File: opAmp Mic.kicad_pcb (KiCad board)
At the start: 2 copper layers, 19 x 80.5 mm, 24 parts, among them J1 XLR3, U1 OPA1642

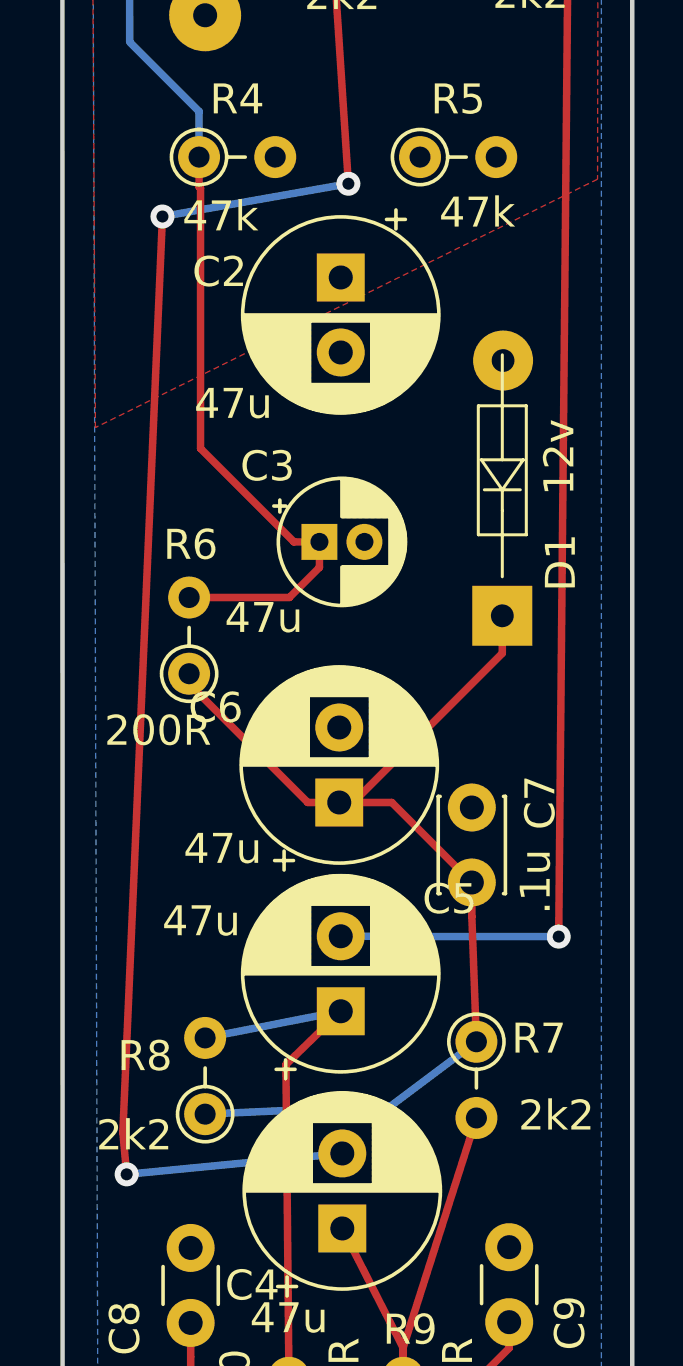
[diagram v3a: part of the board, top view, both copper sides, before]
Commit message: cleaned up 1 trace for only aesthetic reasons
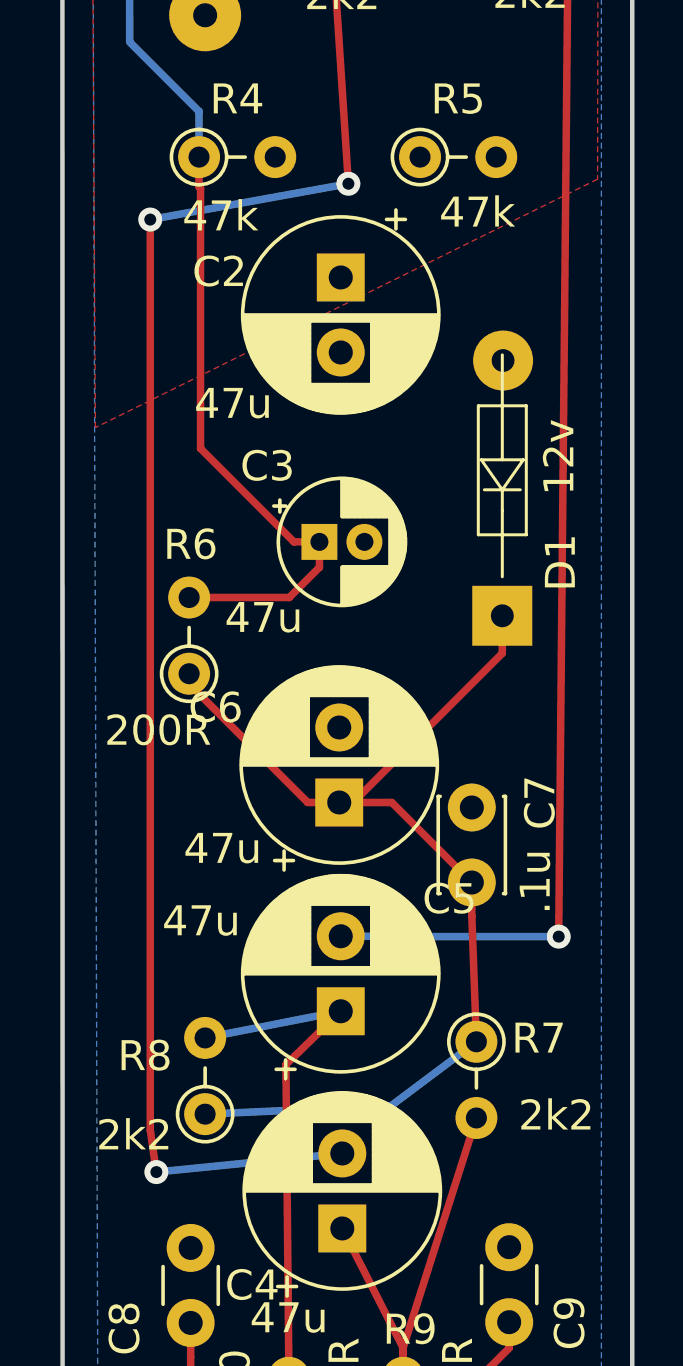
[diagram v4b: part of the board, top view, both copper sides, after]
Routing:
- net Net-(C4-Pad2): track 70.4 -> 69.6 mm
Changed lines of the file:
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@@
   (segment (start 119.507 78.411) (end 119.507 82.423) (width 0.25) (layer F.Cu) (net 4))
   (segment (start 117.348 84.328) (end 117.602 84.328) (width 0.25) (layer B.Cu) (net 4))
-  (via (at 111.6838 125.5522) (size 0.8) (drill 0.4) (layers F.Cu B.Cu) (net 4))
-  (segment (start 111.6838 125.5522) (end 118.872 124.8556) (width 0.25) (layer B.Cu) (net 4))
-  (via (at 112.8776 93.6244) (size 0.8) (drill 0.4) (layers F.Cu B.Cu) (net 4))
-  (segment (start 111.5568 124.1552) (end 111.6838 125.5522) (width 0.25) (layer F.Cu) (net 4))
-  (segment (start 112.8776 93.6244) (end 111.5568 124.1552) (width 0.25) (layer F.Cu) (net 4))
   (segment (start 118.604487 85.330487) (end 117.602 84.328) (width 0.25) (layer F.Cu) (net 4))
   (segment (start 119.0752 92.5322) (end 118.604487 85.330487) (width 0.25) (layer F.Cu) (net 4))
   (via (at 119.0752 92.5322) (size 0.8) (drill 0.4) (layers F.Cu B.Cu) (net 4))
-  (segment (start 112.8776 93.6244) (end 119.0752 92.5322) (width 0.25) (layer B.Cu) (net 4))
+  (via (at 112.6744 125.476) (size 0.8) (drill 0.4) (layers F.Cu B.Cu) (net 4))
+  (segment (start 112.6744 125.476) (end 118.872 124.8556) (width 0.25) (layer B.Cu) (net 4))
+  (segment (start 112.4712 93.726) (end 119.0752 92.5322) (width 0.25) (layer B.Cu) (net 4))
+  (segment (start 112.4712 124.079) (end 112.6744 125.476) (width 0.25) (layer F.Cu) (net 4))
+  (via (at 112.4712 93.726) (size 0.8) (drill 0.4) (layers F.Cu B.Cu) (net 4))
+  (segment (start 112.4712 93.726) (end 112.4712 124.079) (width 0.25) (layer F.Cu) (net 4))
   (segment (start 120.904 131.318) (end 123.3424 123.6726) (width 0.25) (layer F.Cu) (net 5))
   (segment (start 120.904 132.334) (end 120.904 131.318) (width 0.25) (layer F.Cu) (net 5))

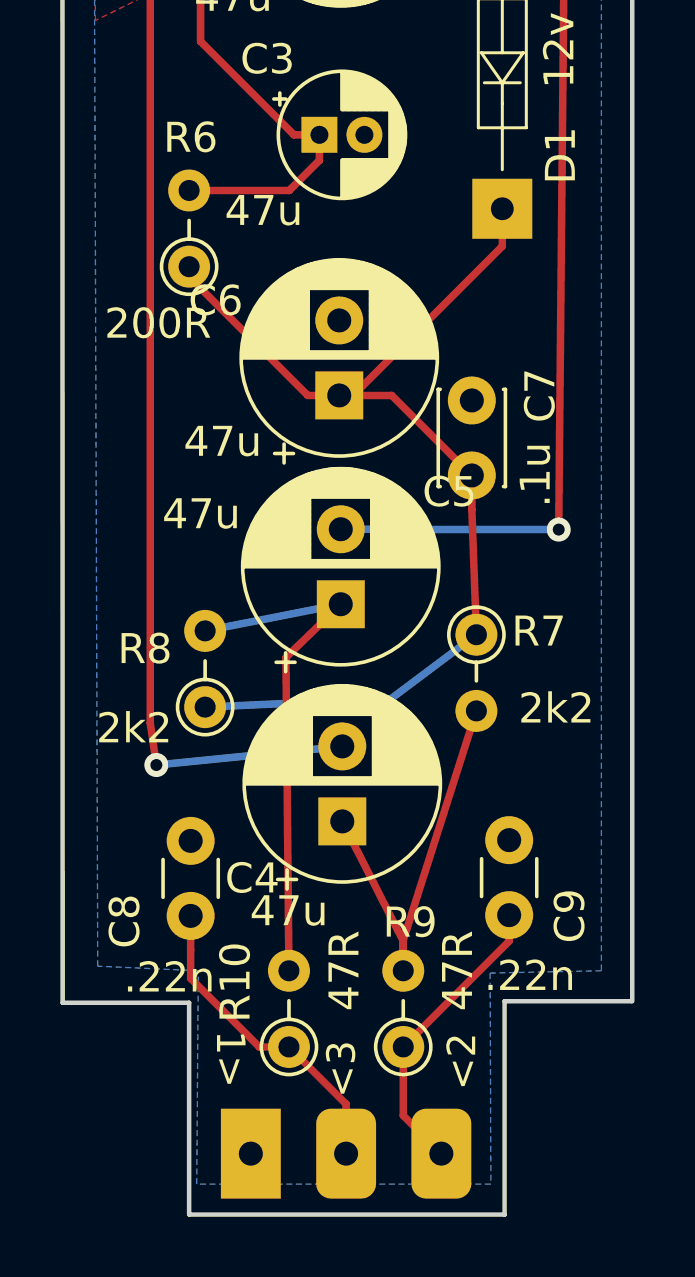
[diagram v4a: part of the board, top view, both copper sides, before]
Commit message: fixed some issues raised by DRC, moved some labels around
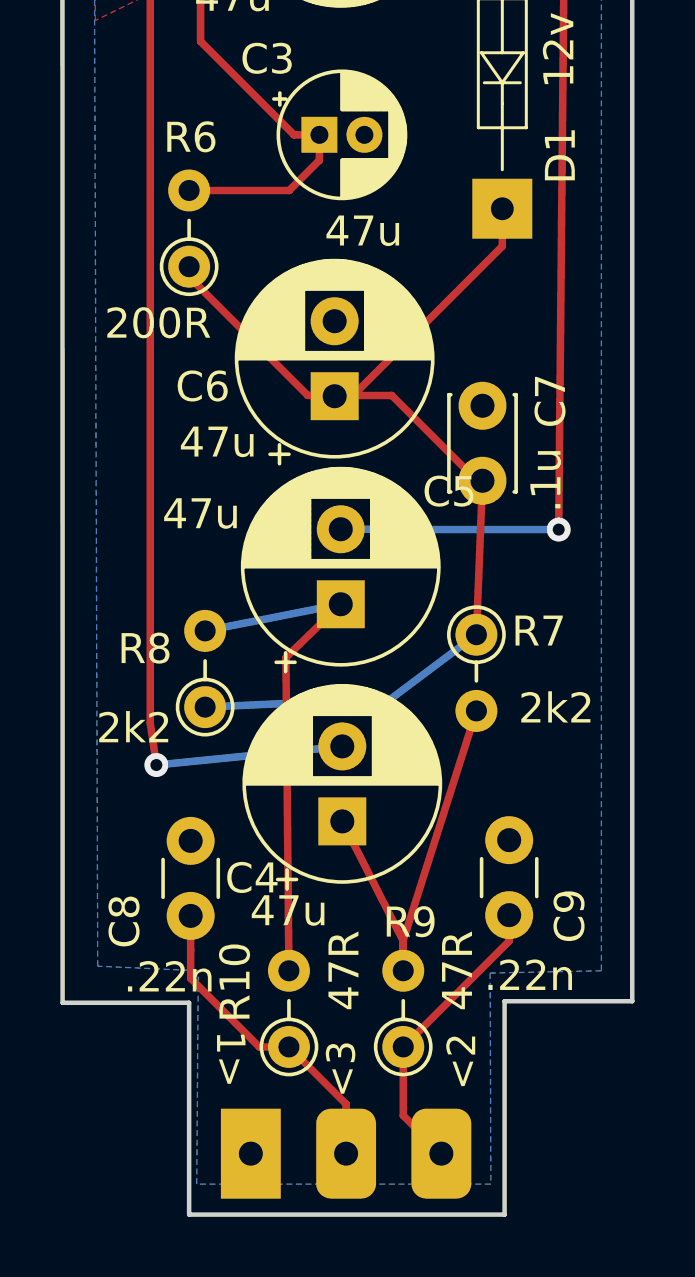
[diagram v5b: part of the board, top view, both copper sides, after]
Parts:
- moved C7 0.40 mm to (123.5, 116.0)
- moved C6 0.15 mm to (118.6, 113.2)
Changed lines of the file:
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@@
   )
   (module Capacitor_THT:C_Disc_D3.0mm_W2.0mm_P2.50mm (layer F.Cu)
-    (at 123.19 115.824 90)
+    (at 123.5456 116.0018 90)
     (descr "C, Disc series, Radial, pin pitch=2.50mm, , diameter*width=3*2mm^2, Capacitor")
     (tags "C Disc series Radial pin pitch 2.50mm  diameter 3mm width 2mm Capacitor")
@@
   )
   (module Capacitor_THT:CP_Radial_D6.3mm_P2.50mm (layer F.Cu)
-    (at 118.7704 113.157 90)
+    (at 118.618 113.1824 90)
     (descr "CP, Radial series, Radial, pin pitch=2.50mm, , diameter=6.3mm, Electrolytic Capacitor")
     (tags "CP Radial series Radial pin pitch 2.50mm  diameter 6.3mm Electrolytic Capacitor")
-    (fp_text reference C6 (at 3.1496 -4.1148 180) (layer F.SilkS)
+    (fp_text reference C6 (at 0.3048 -4.3942 180) (layer F.SilkS)
       (effects (font (size 1 1) (thickness 0.15)))
     )
@@
       (effects (font (size 1 1) (thickness 0.15)))
     )
-    (fp_text value 47u (at -1.8542 2.54) (layer F.SilkS)
+    (fp_text value 47u (at 1.4732 3.2258) (layer F.SilkS)
       (effects (font (size 1 1) (thickness 0.15)))
     )
@@
   (gr_line (start 113.7666 140.462) (end 124.2822 140.462) (layer Edge.Cuts) (width 0.15))
   (gr_line (start 124.2822 133.35) (end 124.2822 140.462) (layer Edge.Cuts) (width 0.15))
-  (gr_line (start 128.5117 133.35) (end 124.2822 133.35) (layer Edge.Cuts) (width 0.15))
+  (gr_line (start 128.5371 133.35) (end 124.2822 133.35) (layer Edge.Cuts) (width 0.15))
   (gr_line (start 113.7666 133.4008) (end 109.5502 133.4008) (layer Edge.Cuts) (width 0.15))
   (gr_text 1> (at 114.6556 135.2804 270) (layer B.SilkS)
@@
     (effects (font (size 0.95 0.95) (thickness 0.1)) (justify bottom))
   )
-  (gr_text "Electret-> OpAmp\nmicrophone platform" (at 125.984 117.9576 90) (layer B.SilkS)
+  (gr_text "Electret-> OpAmp\nmicrophone platform" (at 126.6444 117.9068 90) (layer B.SilkS)
     (effects (font (size 1 1) (thickness 0.15)) (justify mirror))
   )
-  (gr_text "Layout by Chris Williams" (at 111.1504 97.0026 90) (layer B.SilkS)
+  (gr_text "Layout by Chris Williams" (at 111.125 94.488 90) (layer B.SilkS)
     (effects (font (size 2 2) (thickness 0.25)) (justify left mirror))
   )
@@
   (gr_line (start 128.5371 59.9476) (end 128.5371 133.35) (layer Edge.Cuts) (width 0.15))
   (gr_line (start 109.5502 133.4008) (end 109.5371 59.9476) (layer Edge.Cuts) (width 0.15))
-  (gr_line (start 113.7666 133.4008) (end 113.7666 140.4476) (layer Edge.Cuts) (width 0.15))
+  (gr_line (start 113.7666 133.4008) (end 113.7666 140.462) (layer Edge.Cuts) (width 0.15))
   (segment (start 120.347999 71.590001) (end 124.422001 71.590001) (width 0.25) (layer F.Cu) (net 1))
   (segment (start 124.422001 71.590001) (end 125.222 72.39) (width 0.25) (layer F.Cu) (net 1))
@@
   (segment (start 124.206 108.184) (end 119.233 113.157) (width 0.25) (layer F.Cu) (net 8))
   (segment (start 124.206 106.934) (end 124.206 108.184) (width 0.25) (layer F.Cu) (net 8))
-  (segment (start 120.523 113.157) (end 118.7704 113.157) (width 0.25) (layer F.Cu) (net 8))
-  (segment (start 123.19 115.824) (end 120.523 113.157) (width 0.25) (layer F.Cu) (net 8))
   (segment (start 113.7666 109.2032) (end 113.7666 108.8644) (width 0.25) (layer F.Cu) (net 8))
   (segment (start 117.7204 113.157) (end 113.7666 109.2032) (width 0.25) (layer F.Cu) (net 8))
@@
   (segment (start 120.4976 123.2662) (end 123.3424 121.1326) (width 0.25) (layer B.Cu) (net 8))
   (segment (start 114.3 123.5456) (end 120.4976 123.2662) (width 0.25) (layer B.Cu) (net 8))
-  (segment (start 123.19 116.95537) (end 123.3424 121.1326) (width 0.25) (layer F.Cu) (net 8))
-  (segment (start 123.19 115.824) (end 123.19 116.95537) (width 0.25) (layer F.Cu) (net 8))
+  (segment (start 123.19 115.824) (end 123.5456 116.0018) (width 0.25) (layer F.Cu) (net 8))
+  (segment (start 118.7704 113.157) (end 120.523 113.157) (width 0.25) (layer F.Cu) (net 8))
+  (segment (start 123.5456 116.0018) (end 123.3424 121.1326) (width 0.25) (layer F.Cu) (net 8))
+  (segment (start 120.523 113.157) (end 123.19 115.824) (width 0.25) (layer F.Cu) (net 8))
   (segment (start 118.999 136.779) (end 117.094 134.874) (width 0.25) (layer F.Cu) (net 9))
   (segment (start 118.999 138.43) (end 118.999 136.779) (width 0.25) (layer F.Cu) (net 9))

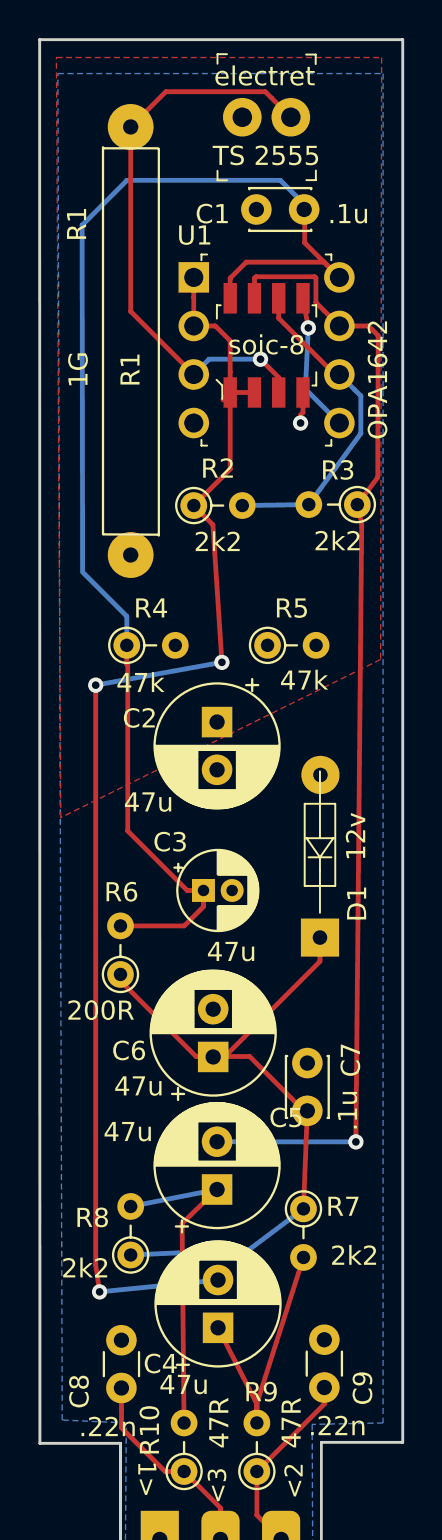
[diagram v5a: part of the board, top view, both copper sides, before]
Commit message: moved op amp, changed current paths , enlarged and shortened high impedence nets
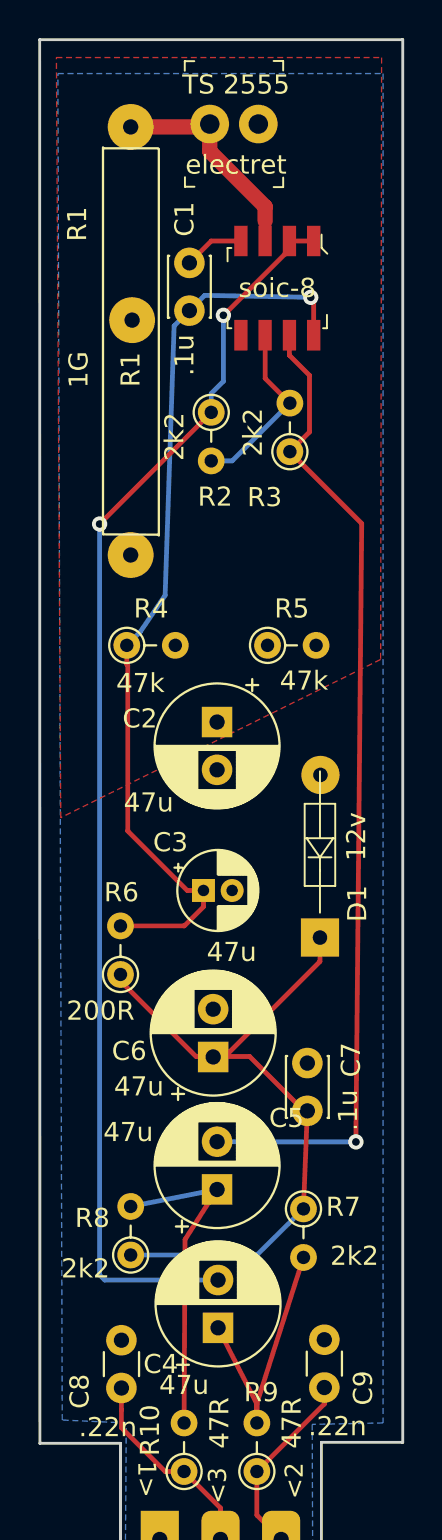
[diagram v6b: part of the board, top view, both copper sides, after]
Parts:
- removed U1: OPA1642, digikey:DIP-8_W7.62mm
- moved R2 4.96 mm to (118.5, 79.5), turned to 270 degrees
- moved R3 4.49 mm to (122.6, 81.5), turned to 90 degrees
- moved C1 4.48 mm to (117.4, 71.6), turned to 270 degrees
- moved soic-8 3.05 mm to (122.0, 72.9), turned to 270 degrees
- moved TS 2555 0.91 mm to (121.0, 64.4), turned to 180 degrees
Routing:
- net Net-(C1-Pad2): track 68.7 -> 47.9 mm, vias 0 -> 1
- net Net-(MK1-Pad2): track 30.0 -> 12.0 mm, vias 1 -> 0
- net Net-(R2-Pad2): track 17.1 -> 9.46 mm
- net GND: track 7.53 -> 0.00 mm, vias 1 -> 0
- net Net-(C5-Pad2): track 59.4 -> 51.9 mm
- net Net-(C4-Pad2): track 69.6 -> 65.7 mm, vias 3 -> 2
- net Earth: track 1.65 -> 3.17 mm, vias 1 -> 0
